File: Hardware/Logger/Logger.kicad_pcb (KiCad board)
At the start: 2 copper layers, 70 x 70 mm, 56 parts, among them CN1 Conn_02x19_Odd_Even, CN10 Conn_02x19_Odd_Even, CN2 Conn_02x19_Odd_Even, CN7 Conn_02x19_Odd_Even, J1 Conn_Coaxial, J2 Conn_Coaxial, J3 Conn_Coaxial, J4 Conn_Coaxial, J5 Conn_01x04_Female, J6 SD_Card, J7 DB9_Female_MountingHoles, Q1 FDV304P, Q2 FDV304P, SW1 SW_Push, SW2 SW_Push, SW3 SW_Push, SW4 SW_Push, U1 ESP-12E, U2 ST7735S

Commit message: fix #27, fix #30, fix #32
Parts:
- removed JP1, JP2, JP3, JP4: Jumper_NO_Small, Jumper:SolderJumper-2_P1.3mm_Open_Pad1.0x1.5mm
- removed R13: 10k, Resistor_SMD:R_0402_1005Metric
- removed R19, R20: 0R, Resistor_SMD:R_0402_1005Metric
- added C10: 330n, Capacitor_SMD:C_0402_1005Metric, F.Cu at (165.8, 88.4)
- added C11: 330n, Capacitor_SMD:C_0402_1005Metric, F.Cu at (168.7, 86.5)
- added C8: 330n, Capacitor_SMD:C_0402_1005Metric, F.Cu at (170.9, 69.0)
- added C9: 330n, Capacitor_SMD:C_0402_1005Metric, F.Cu at (165.8, 86.5)
- added J10: Conn_01x08_Female, Connector_PinSocket_2.54mm:PinSocket_1x08_P2.54mm_Vertical, F.Cu at (168.9, 112.0)
- added J8: Conn_01x06_Female, Connector_PinSocket_2.54mm:PinSocket_1x06_P2.54mm_Vertical, F.Cu at (164.4, 94.1)
- added J9: Conn_01x08_Female, Connector_PinSocket_2.54mm:PinSocket_1x08_P2.54mm_Vertical, F.Cu at (145.0, 111.9)
- added U3: LD1117ASTR, Package_TO_SOT_SMD:SOT-223, F.Cu at (165.8, 70.1)
- C1, C2, C3, C4: value 47n -> 330n; footprint Capacitor_SMD:C_0805_2012Metric -> Capacitor_SMD:C_0402_1005Metric
- C5: value 100n -> 330n
- J5: value Conn_01x04_Female -> USB_B_Micro; footprint Connector_PinHeader_2.54mm:PinHeader_1x04_P2.54mm_Vertical -> Connector_USB:USB_Micro-B_Molex-105017-0001
- R4: value 1k -> R_PHOTO; footprint Resistor_SMD:R_0805_2012Metric -> OptoDevice:R_LDR_7x6mm_P5.1mm_Vertical
- R7, R8: value 1k -> TBD; footprint Resistor_SMD:R_0805_2012Metric -> Resistor_SMD:R_0402_1005Metric
- moved R3 50.4 mm to (232.0, 121.6), turned to 0 degrees
- moved R4 46.3 mm to (222.7, 123.9), turned to 0 degrees
- moved C1 29.8 mm to (171.8, 83.4)
- moved C2 25.6 mm to (169.8, 77.6)
- moved C5 22.5 mm to (170.9, 71.9), turned to 90 degrees
- moved J5 21.3 mm to (164.6, 79.9), turned to 90 degrees
- moved D2 15.3 mm to (145.6, 77.5)
- moved Q2 15.3 mm to (146.1, 74.3)
- moved R17 15.3 mm to (148.5, 77.5)
- moved R23 15.3 mm to (151.4, 77.2)
- moved C7 15.3 mm to (151.4, 79.1)
- moved D1 15.3 mm to (150.1, 73.2)
- moved R16 15.3 mm to (153.0, 73.2)
- moved R21 15.3 mm to (148.3, 79.5)
- moved C3 15.0 mm to (171.8, 77.6)
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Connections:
- C1 pad 1: Net-(C1-Pad1) -> 5V
- C2 pad 1: Net-(C2-Pad1) -> 5V
- C3 pad 1: Net-(C3-Pad1) -> 5V
- C4 pad 1: Net-(C4-Pad1) -> 3V3
- C5 pad 1: Net-(C5-Pad1) -> 3V3
- C6 pad 1: Net-(C5-Pad1) -> /WiFiInterface/ESP_VCC
- C7 pad 1: Net-(C5-Pad1) -> /WiFiInterface/ESP_VCC
- CN1 pad 18: Net-(CN1-Pad18) -> 5V
- CN7 pad 17: Net-(CN1-Pad18) -> 5V
- D1 pad 2: (no net) -> /WiFiInterface/GPIO16
- D2 pad 2: (no net) -> /WiFiInterface/GPIO15
- J5 pad 1: GND -> 5V
- J5 pad 2: Net-(J5-Pad2) -> (no net)
- J5 pad 3: Net-(J5-Pad3) -> (no net)
- J5 pad 4: Net-(C5-Pad1) -> (no net)
- Q1 pad 2: Net-(Q1-Pad2) -> VCC
- Q1 pad 3: Net-(C5-Pad1) -> /WiFiInterface/ESP_VCC
- Q2 pad 2: Net-(Q1-Pad2) -> VCC
- R1 pad 2: Net-(JP1-Pad1) -> KEY_UP
- R14 pad 1: Net-(C5-Pad1) -> /WiFiInterface/ESP_VCC
- R14 pad 2: (no net) -> ESP_FLASH_MODE
- R15 pad 2: Net-(R15-Pad2) -> /WiFiInterface/TXD
- R16 pad 2: Net-(R16-Pad2) -> /WiFiInterface/RXD
- R17 pad 1: Net-(C5-Pad1) -> /WiFiInterface/ESP_VCC
- R17 pad 2: (no net) -> /WiFiInterface/EN
- R18 pad 1: Net-(C5-Pad1) -> /WiFiInterface/ESP_VCC
- R18 pad 2: (no net) -> /WiFiInterface/RST
- R2 pad 2: Net-(JP2-Pad1) -> KEY_DOWN
- R3 pad 1: Net-(JP1-Pad1) -> VCC
- R3 pad 2: Net-(C1-Pad1) -> LIGHT_PROBE
- R4 pad 1: Net-(JP2-Pad1) -> LIGHT_PROBE
- R4 pad 2: Net-(C2-Pad1) -> GND
- R5 pad 2: Net-(JP3-Pad1) -> KEY_LEFT
- R6 pad 2: Net-(JP4-Pad1) -> KEY_RIGHT
- R7 pad 1: Net-(JP3-Pad1) -> 3V3
- R7 pad 2: Net-(C3-Pad1) -> Net-(C10-Pad1)
- R8 pad 1: Net-(JP4-Pad1) -> Net-(C10-Pad1)
- R8 pad 2: Net-(C4-Pad1) -> GND
- SW1 pad 2: Net-(JP1-Pad1) -> KEY_UP
- SW2 pad 2: Net-(JP2-Pad1) -> KEY_DOWN
- SW3 pad 2: Net-(JP3-Pad1) -> KEY_LEFT
- SW4 pad 2: Net-(JP4-Pad1) -> KEY_RIGHT
- U1 pad 1: (no net) -> /WiFiInterface/RST
- U1 pad 10: (no net) -> MISO
- U1 pad 11: (no net) -> /WiFiInterface/GPIO9
- U1 pad 12: (no net) -> /WiFiInterface/GPIO10
- U1 pad 13: (no net) -> MOSI
- U1 pad 14: (no net) -> SCK
- U1 pad 15: (no net) -> GND
- U1 pad 16: (no net) -> /WiFiInterface/GPIO15
- U1 pad 17: (no net) -> /WiFiInterface/GPIO12
- U1 pad 18: (no net) -> ESP_FLASH_MODE
- U1 pad 19: (no net) -> /WiFiInterface/GPIO4
- U1 pad 2: (no net) -> /WiFiInterface/ADC
- U1 pad 20: (no net) -> /WiFiInterface/GPIO5
- U1 pad 21: (no net) -> /WiFiInterface/RXD
- U1 pad 22: (no net) -> /WiFiInterface/TXD
- U1 pad 3: (no net) -> /WiFiInterface/EN
- U1 pad 4: (no net) -> /WiFiInterface/GPIO16
- U1 pad 5: (no net) -> /WiFiInterface/GPIO14
- U1 pad 6: (no net) -> /WiFiInterface/GPIO12
- U1 pad 7: (no net) -> /WiFiInterface/GPIO13
- U1 pad 8: (no net) -> /WiFiInterface/ESP_VCC
- U1 pad 9: (no net) -> CS_ESP

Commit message: fix #38
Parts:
- added C12: 330n, Capacitor_SMD:C_0402_1005Metric, B.Cu at (185.1, 105.6)
- added C13: 330n, Capacitor_SMD:C_0402_1005Metric, B.Cu at (182.2, 105.6)
- added C14: 330n, Capacitor_SMD:C_0402_1005Metric, B.Cu at (179.4, 105.6)
- added R13: 10k, Resistor_SMD:R_0805_2012Metric, B.Cu at (184.3, 100.2)
- added R19: 10k, Resistor_SMD:R_0805_2012Metric, B.Cu at (184.3, 103.2)
- added R20: 10k, Resistor_SMD:R_0805_2012Metric, B.Cu at (179.9, 100.2)
- added R25: 10k, Resistor_SMD:R_0805_2012Metric, B.Cu at (179.9, 103.2)
- added R26: 10k, Resistor_SMD:R_0805_2012Metric, B.Cu at (175.5, 100.2)
- added R27: 10k, Resistor_SMD:R_0805_2012Metric, B.Cu at (175.5, 103.2)
- J6: value SD_Card -> 112K-TAA0-RA1_ATTEND; footprint Connector_Card:microSD_HC_Hirose_DM3BT-DSF-PEJS -> Logger:104B-TAA0-R_ATTEND
- moved R4 107.8 mm to (131.9, 65.8)
- moved R3 103.4 mm to (144.4, 66.8), turned to 90 degrees
- moved J6 23.3 mm to (186.1, 109.6)
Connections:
- J6 pad 1: (no net) -> Net-(J6-Pad1)
- J6 pad 10: (no net) -> GND
- J6 pad 2: (no net) -> CS_SD
- J6 pad 3: (no net) -> MOSI
- J6 pad 4: (no net) -> 3V3
- J6 pad 5: (no net) -> SCK
- J6 pad 6: (no net) -> GND
- J6 pad 7: (no net) -> MISO
- J6 pad 8: (no net) -> Net-(J6-Pad8)
- J6 pad 9: (no net) -> GND

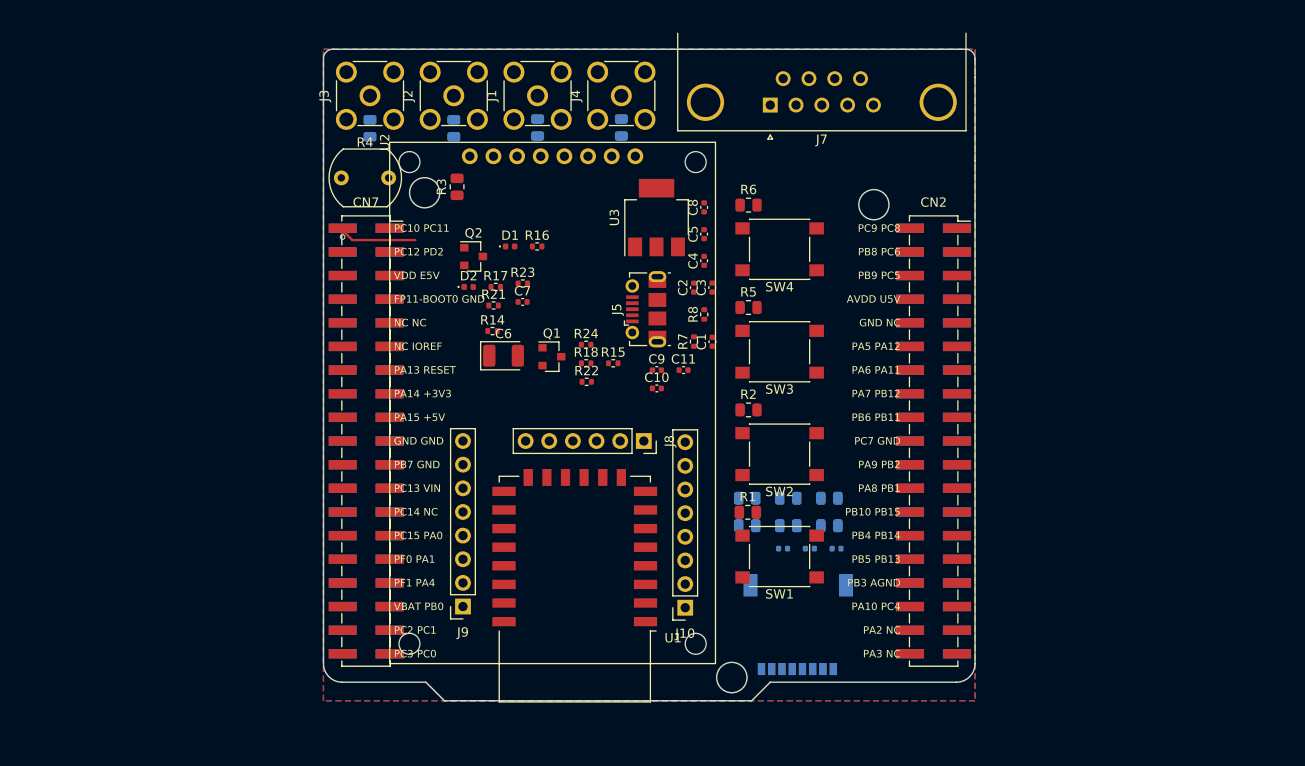
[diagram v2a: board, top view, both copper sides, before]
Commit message: switched to kicad6, finished circuit and component placement on pcb
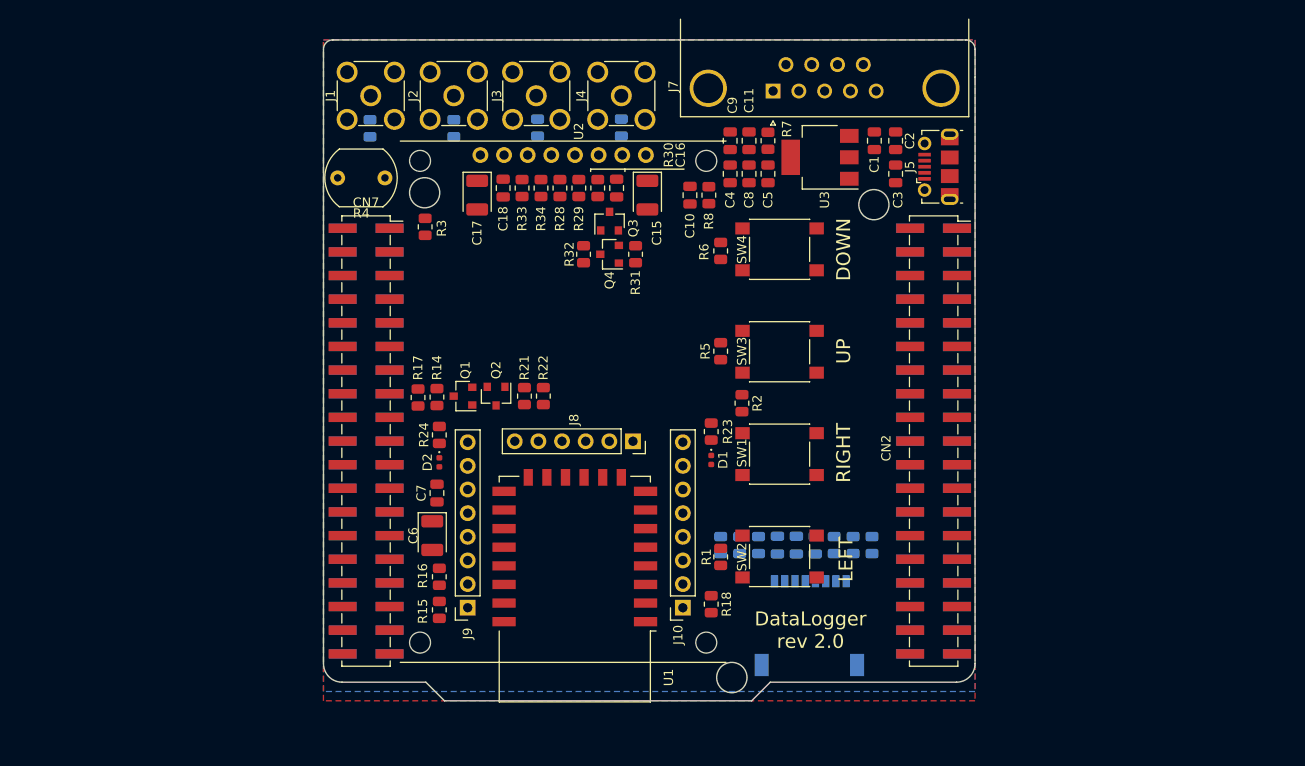
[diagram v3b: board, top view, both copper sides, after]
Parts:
- added C15: 47u/6V3, Capacitor_Tantalum_SMD:CP_EIA-3528-21_Kemet-B, F.Cu at (164.8, 67.7)
- added C16: 100n, Capacitor_SMD:C_0805_2012Metric, F.Cu at (161.5, 66.9)
- added C17: 47u/6V3, Capacitor_Tantalum_SMD:CP_EIA-3528-21_Kemet-B, F.Cu at (146.5, 67.7)
- added C18: 100n, Capacitor_SMD:C_0805_2012Metric, F.Cu at (149.3, 66.9)
- added Q3: FDV304P, Package_TO_SOT_SMD:SOT-23, F.Cu at (160.7, 70.5)
- added Q4: FDV304P, Package_TO_SOT_SMD:SOT-23, F.Cu at (160.7, 74.0)
- added R28: 1k, Resistor_SMD:R_0805_2012Metric, F.Cu at (155.4, 66.9)
- added R29: 0R, Resistor_SMD:R_0805_2012Metric, F.Cu at (157.4, 66.9)
- added R30: 0R, Resistor_SMD:R_0805_2012Metric, F.Cu at (159.5, 66.9)
- added R31: 1k, Resistor_SMD:R_0805_2012Metric, F.Cu at (163.5, 74.0)
- added R32: 1k, Resistor_SMD:R_0805_2012Metric, F.Cu at (157.9, 74.0)
- added R33: 0R, Resistor_SMD:R_0805_2012Metric, F.Cu at (151.3, 66.9)
- added R34: 0R, Resistor_SMD:R_0805_2012Metric, F.Cu at (153.4, 66.9)
- C1, C10, C11, C12, C13, C14, C2, C3, C4, C5, C7, C8, C9: footprint Capacitor_SMD:C_0402_1005Metric -> Capacitor_SMD:C_0805_2012Metric
- R11, R12, R9: value 1k -> 100R
- R14, R15, R16, R17, R18, R21, R22, R23, R24, R7, R8: footprint Resistor_SMD:R_0402_1005Metric -> Resistor_SMD:R_0805_2012Metric
- moved R16 37.0 mm to (142.4, 108.7), turned to -90 degrees
- moved J5 34.9 mm to (196.0, 64.6)
- moved R15 32.4 mm to (142.4, 112.2), turned to -90 degrees
- moved D1 31.5 mm to (171.7, 96.1), turned to -90 degrees
- moved R18 29.2 mm to (171.7, 111.6), turned to -90 degrees
- moved C1 27.7 mm to (189.2, 61.8)
- moved C2 26.8 mm to (191.5, 61.8)
- moved C9 25.9 mm to (173.7, 61.8), turned to -90 degrees
- moved R23 25.7 mm to (171.7, 93.1), turned to 90 degrees
- moved C11 25.6 mm to (175.7, 61.8), turned to -90 degrees
- moved C3 23.2 mm to (191.5, 65.4), turned to -90 degrees
- moved R7 23.0 mm to (177.8, 61.8)
- moved C7 22.5 mm to (142.2, 99.7), turned to 90 degrees
- moved C10 21.1 mm to (169.4, 67.7), turned to -90 degrees
- moved C6 20.8 mm to (141.7, 104.3), turned to -90 degrees
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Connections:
- net Net-(CN10-Pad10) renamed CS_LCD
- net Net-(CN10-Pad12) renamed DC_LCD
- CN1 pad 37: (no net) -> Net-(CN1-Pad37)
- CN10 pad 13: Net-(CN10-Pad13) -> MISO
- CN10 pad 14: Net-(CN10-Pad14) -> ESP_TX
- CN10 pad 15: Net-(CN10-Pad15) -> MOSI
- CN10 pad 16: Net-(CN10-Pad16) -> ESP_RX
- CN10 pad 18: Net-(CN10-Pad18) -> CS_ESP
- CN10 pad 20: Net-(CN10-Pad20) -> ESP_FLASH_MODE
- CN10 pad 22: Net-(CN10-Pad22) -> ESP_ENABLE
- CN10 pad 24: Net-(CN10-Pad24) -> KEY_RIGHT
- CN10 pad 26: Net-(CN10-Pad26) -> KEY_LEFT
- CN10 pad 28: Net-(CN10-Pad28) -> KEY_DOWN
- CN10 pad 30: Net-(CN10-Pad30) -> KEY_UP
- CN10 pad 31: Net-(CN10-Pad31) -> SCK
- CN10 pad 32: Net-(CN10-Pad32) -> ANALOG_IN_1
- CN10 pad 34: Net-(CN10-Pad34) -> ANALOG_IN_2
- CN10 pad 36: Net-(CN10-Pad36) -> ANALOG_IN_3
- CN10 pad 38: Net-(CN10-Pad38) -> ANALOG_IN_4
- CN10 pad 6: Net-(CN10-Pad6) -> EXT_TX
- CN10 pad 8: Net-(CN10-Pad8) -> EXT_RX
- CN2 pad 13: Net-(CN10-Pad14) -> ESP_TX
- CN2 pad 14: Net-(CN10-Pad13) -> MISO
- CN2 pad 15: Net-(CN10-Pad16) -> ESP_RX
- CN2 pad 16: Net-(CN10-Pad15) -> MOSI
- CN2 pad 17: Net-(CN10-Pad18) -> CS_ESP
- CN2 pad 19: Net-(CN10-Pad20) -> ESP_FLASH_MODE
- CN2 pad 21: Net-(CN10-Pad22) -> ESP_ENABLE
- CN2 pad 23: Net-(CN10-Pad24) -> KEY_RIGHT
- CN2 pad 25: Net-(CN10-Pad26) -> KEY_LEFT
- CN2 pad 27: Net-(CN10-Pad28) -> KEY_DOWN
- CN2 pad 29: Net-(CN10-Pad30) -> KEY_UP
- CN2 pad 31: Net-(CN10-Pad32) -> ANALOG_IN_1
- CN2 pad 32: Net-(CN10-Pad31) -> SCK
- CN2 pad 33: Net-(CN10-Pad34) -> ANALOG_IN_2
- CN2 pad 35: Net-(CN10-Pad36) -> ANALOG_IN_3
- CN2 pad 37: Net-(CN10-Pad38) -> ANALOG_IN_4
- CN2 pad 5: Net-(CN10-Pad6) -> EXT_TX
- CN2 pad 7: Net-(CN10-Pad8) -> EXT_RX
- CN7 pad 38: (no net) -> Net-(CN1-Pad37)
- J7 pad 0: Net-(J7-Pad0) -> GND
- J7 pad 2: (no net) -> EXT_RX
- J7 pad 3: (no net) -> EXT_TX
- Q1 pad 2: VCC -> 3V3
- Q2 pad 2: VCC -> 3V3
- R1 pad 1: VCC -> 3V3
- R10 pad 2: (no net) -> ANALOG_IN_2
- R11 pad 2: (no net) -> ANALOG_IN_3
- R12 pad 2: (no net) -> ANALOG_IN_4
- R15 pad 1: (no net) -> ESP_TX
- R16 pad 1: (no net) -> ESP_RX
- R2 pad 1: VCC -> 3V3
- R3 pad 1: VCC -> 3V3
- R5 pad 1: VCC -> 3V3
- R6 pad 1: VCC -> 3V3
- R9 pad 2: (no net) -> ANALOG_IN_1
- U2 pad 1: (no net) -> GND
- U2 pad 2: (no net) -> 3V3
- U2 pad 3: (no net) -> Net-(R33-Pad2)
- U2 pad 4: (no net) -> Net-(R34-Pad2)
- U2 pad 5: (no net) -> Net-(R28-Pad2)
- U2 pad 6: (no net) -> Net-(R29-Pad2)
- U2 pad 7: (no net) -> Net-(R30-Pad2)
- U2 pad 8: (no net) -> /UserInterface/LCD_BACKLIGHT
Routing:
- net Net-(CN1-Pad1): track 9.41 -> 0.00 mm, vias 1 -> 0
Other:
- board size 70 x 70 mm -> 70 x 71 mm
- net class Default removed
- board text added: "DOWN"
- board text added: "DataLogger rev 2.0"
- board text added: "LEFT"
- board text added: "RIGHT"
- board text added: "UP"

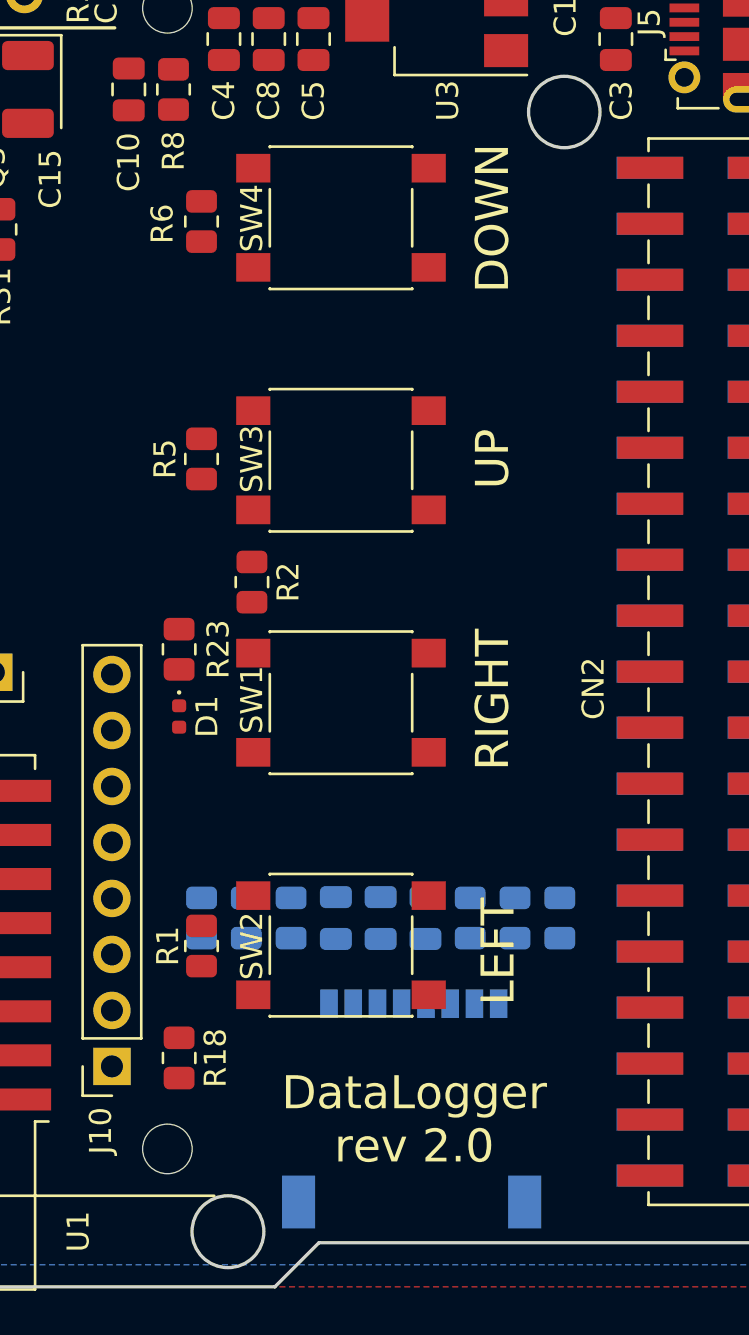
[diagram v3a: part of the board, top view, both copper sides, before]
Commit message: add on silkscreen icons to describe purpouse of buttons
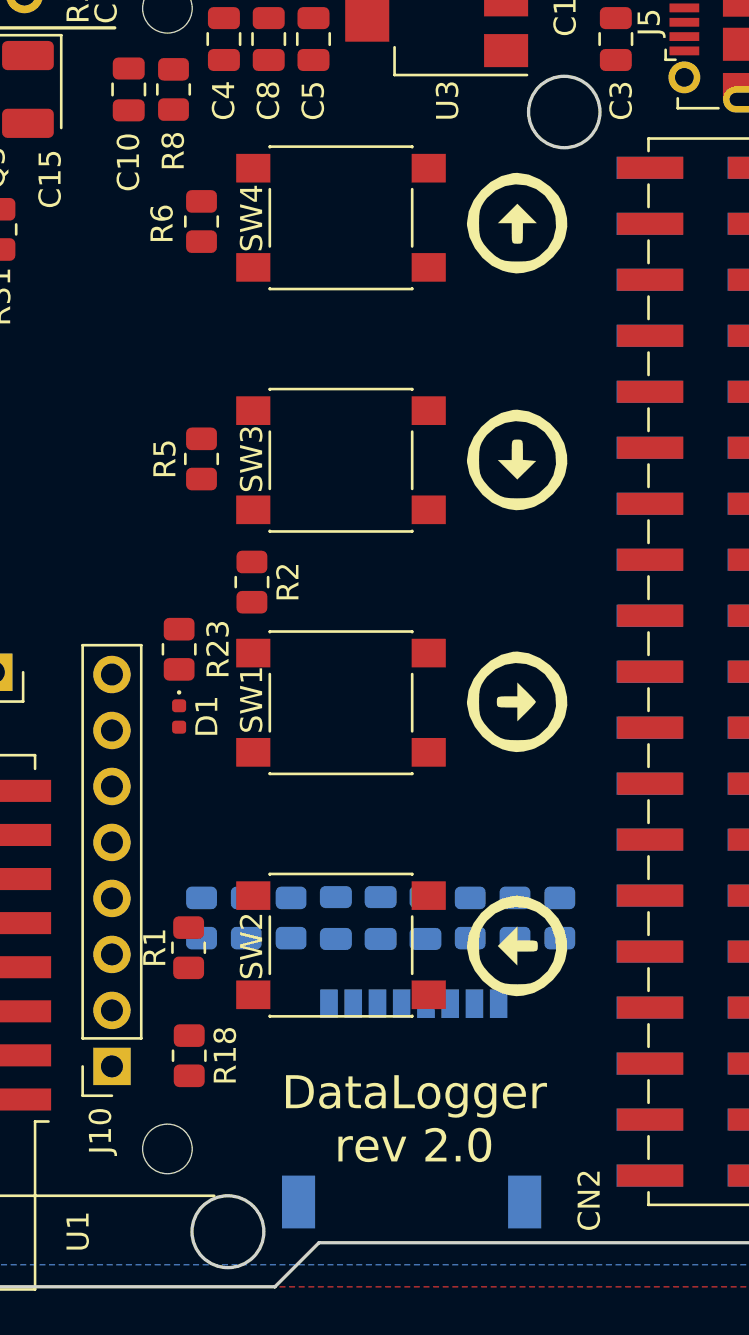
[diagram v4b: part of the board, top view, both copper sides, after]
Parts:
- added G***: LOGO, Logger:arrow-right-circle-line, F.Cu at (187.0, 73.7)
- added G***: LOGO, Logger:arrow-up-circle-line, F.Cu at (187.0, 106.5)
- added G***: LOGO, Logger:arrow-left-circle-line, F.Cu at (187.0, 84.5)
- added G***: LOGO, Logger:arrow-down-circle-line, F.Cu at (187.0, 95.5)
- moved R1 0.59 mm to (172.1, 106.6)
- moved R18 0.47 mm to (172.1, 111.5)
- renumbered R10 to R100R1
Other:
- board text removed: "DOWN"
- board text removed: "LEFT"
- board text removed: "RIGHT"
- board text removed: "UP"

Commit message: fix #41
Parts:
- added Q5: BC848, Package_TO_SOT_SMD:SOT-23, B.Cu at (147.0, 68.7)
- added Q6: BC848, Package_TO_SOT_SMD:SOT-23, B.Cu at (152.6, 68.7)
- added Q7: BC848, Package_TO_SOT_SMD:SOT-23, B.Cu at (158.2, 68.7)
- added Q8: BC848, Package_TO_SOT_SMD:SOT-23, B.Cu at (163.8, 68.7)
- added R10: 8k2, Resistor_SMD:R_0805_2012Metric, B.Cu at (144.2, 68.7)
- added R35: 8k2, Resistor_SMD:R_0805_2012Metric, B.Cu at (149.8, 68.7)
- added R36: 100R, Resistor_SMD:R_0805_2012Metric, B.Cu at (181.1, 59.8)
- added R37: 100R, Resistor_SMD:R_0805_2012Metric, B.Cu at (183.8, 59.8)
- added R38: 8k2, Resistor_SMD:R_0805_2012Metric, B.Cu at (155.4, 68.7)
- added R39: 8k2, Resistor_SMD:R_0805_2012Metric, B.Cu at (161.0, 68.7)
- moved R9 18.0 mm to (135.0, 60.3)
- moved R11 17.9 mm to (152.9, 60.2)
- renumbered R100R1 to R10
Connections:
- J7 pad 2: EXT_RX -> Net-(J7-Pad2)
- J7 pad 3: EXT_TX -> Net-(J7-Pad3)
- R10 pad 2: ANALOG_IN_2 -> Net-(R100R1-Pad2)
- R11 pad 2: ANALOG_IN_3 -> Net-(R11-Pad2)
- R12 pad 2: ANALOG_IN_4 -> Net-(R12-Pad2)
- R9 pad 2: ANALOG_IN_1 -> Net-(Q5-Pad1)
